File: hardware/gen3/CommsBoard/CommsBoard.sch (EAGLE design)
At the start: 47 parts, among them M5LOCK IMU_HEADER, U1 ATMEGA165PV-8AU

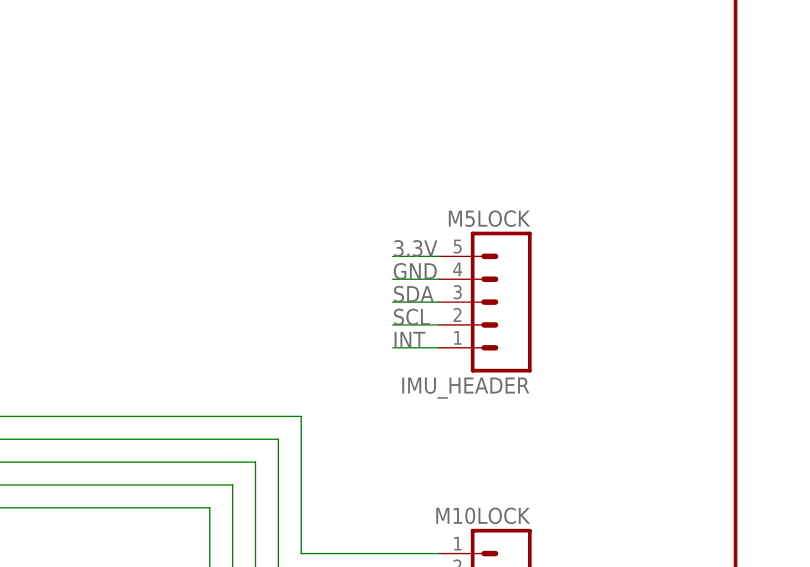
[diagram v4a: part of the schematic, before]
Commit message: Added IMU package
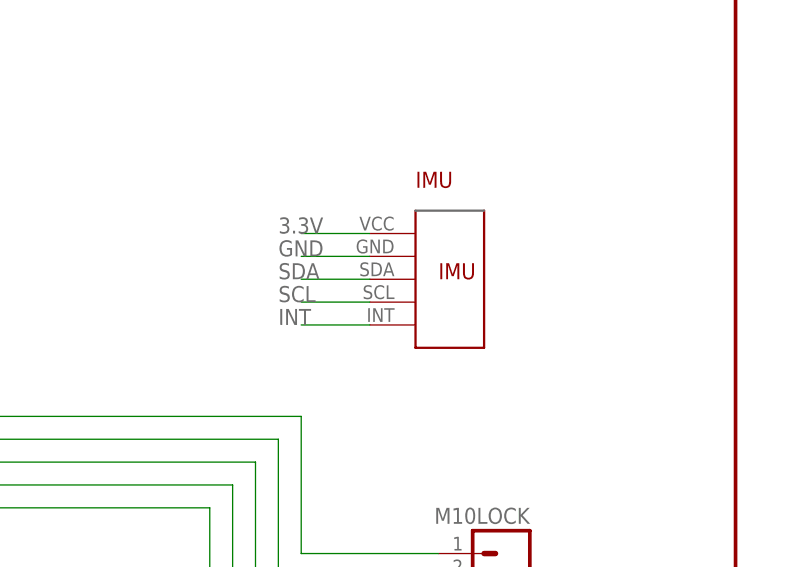
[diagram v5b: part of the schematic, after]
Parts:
- removed M5LOCK: IMU_HEADER, SparkFun-Connectors:M05LOCK
- added IMU: MPU6050IMUMPU, gen3:MPU6050IMUMPU
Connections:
- net 3.3V: now also IMU.VCC; no longer M5LOCK.5
- net GND: now also IMU.GND; no longer M5LOCK.4
- net INT: now also IMU.INT; no longer M5LOCK.1
- net SCL: now also IMU.SCL; no longer M5LOCK.2
- net SDA: now also IMU.SDA; no longer M5LOCK.3
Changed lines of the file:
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@@
 <part name="S1" library="SparkFun-Electromechanical" deviceset="SWITCH-MOMENTARY-2" device="SMD-4"/>
 <part name="R21" library="SparkFun-Passives" deviceset="RESISTOR" device="0805-RES" value="10k"/>
-<part name="M5LOCK" library="SparkFun-Connectors" deviceset="M05" device="LOCK" value="IMU_HEADER"/>
+<part name="IMU" library="gen3" deviceset="MPU6050IMU" device="MPU"/>
 </parts>
 <sheets>
@@
 <instance part="S1" gate="G$1" x="170.18" y="144.78"/>
 <instance part="R21" gate="G$1" x="172.72" y="132.08"/>
-<instance part="M5LOCK" gate="G$1" x="223.52" y="93.98" rot="MR0"/>
+<instance part="IMU" gate="G$1" x="215.9" y="96.52"/>
 </instances>
 <busses>
@@
 </segment>
 <segment>
-<pinref part="M5LOCK" gate="G$1" pin="4"/>
-<wire x1="215.9" y1="96.52" x2="210.82" y2="96.52" width="0.1524" layer="91"/>
-<label x="210.82" y="96.52" size="1.778" layer="95"/>
+<pinref part="IMU" gate="G$1" pin="GND"/>
+<wire x1="208.28" y1="99.06" x2="200.66" y2="99.06" width="0.1524" layer="91"/>
+<label x="198.12" y="99.06" size="1.778" layer="95"/>
 </segment>
 </net>
@@
 </segment>
 <segment>
-<pinref part="M5LOCK" gate="G$1" pin="5"/>
-<wire x1="215.9" y1="99.06" x2="210.82" y2="99.06" width="0.1524" layer="91"/>
-<label x="210.82" y="99.06" size="1.778" layer="95"/>
+<pinref part="IMU" gate="G$1" pin="VCC"/>
+<wire x1="208.28" y1="101.6" x2="200.66" y2="101.6" width="0.1524" layer="91"/>
+<label x="198.12" y="101.6" size="1.778" layer="95"/>
 </segment>
 </net>
@@
 </segment>
 <segment>
-<pinref part="M5LOCK" gate="G$1" pin="1"/>
-<wire x1="215.9" y1="88.9" x2="210.82" y2="88.9" width="0.1524" layer="91"/>
-<label x="210.82" y="88.9" size="1.778" layer="95"/>
+<pinref part="IMU" gate="G$1" pin="INT"/>
+<wire x1="208.28" y1="91.44" x2="200.66" y2="91.44" width="0.1524" layer="91"/>
+<label x="198.12" y="91.44" size="1.778" layer="95"/>
 </segment>
 </net>
@@
 </segment>
 <segment>
-<pinref part="M5LOCK" gate="G$1" pin="2"/>
-<wire x1="215.9" y1="91.44" x2="210.82" y2="91.44" width="0.1524" layer="91"/>
-<label x="210.82" y="91.44" size="1.778" layer="95"/>
+<pinref part="IMU" gate="G$1" pin="SCL"/>
+<wire x1="208.28" y1="93.98" x2="200.66" y2="93.98" width="0.1524" layer="91"/>
+<label x="198.12" y="93.98" size="1.778" layer="95"/>
 </segment>
 </net>
@@
 </segment>
 <segment>
-<pinref part="M5LOCK" gate="G$1" pin="3"/>
-<wire x1="215.9" y1="93.98" x2="210.82" y2="93.98" width="0.1524" layer="91"/>
-<label x="210.82" y="93.98" size="1.778" layer="95"/>
-</segment>
-</net>
+<pinref part="IMU" gate="G$1" pin="SDA"/>
+<wire x1="208.28" y1="96.52" x2="200.66" y2="96.52" width="0.1524" layer="91"/>
+<label x="198.12" y="96.52" size="1.778" layer="95"/>
+</segment>
+</net>

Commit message: finalized comms board
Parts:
- added C3, C4: 100uF, gen3:CAP-POLAR
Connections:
- net 3.3V: now also C3.+
- net 5V: now also C4.+
- net GND: now also C3.-, C4.-
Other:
- moved on the sheet: C5, C6
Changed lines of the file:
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@@
 <?xml version="1.0" encoding="utf-8"?>
 <!DOCTYPE eagle SYSTEM "eagle.dtd">
-<eagle version="7.2.0">
+<eagle version="6.4">
 <drawing>
 <settings>
@@
 <part name="R21" library="SparkFun-Passives" deviceset="RESISTOR" device="0805-RES" value="10k"/>
 <part name="IMU" library="gen3" deviceset="MPU6050IMU" device="MPU"/>
+<part name="C3" library="gen3" deviceset="CAP-POLAR" device="" value="100uF"/>
+<part name="C4" library="gen3" deviceset="CAP-POLAR" device="" value="100uF"/>
 </parts>
 <sheets>
@@
 <instance part="U1" gate="A" x="129.54" y="106.68"/>
 <instance part="JP1" gate="G$1" x="76.2" y="38.1"/>
-<instance part="C5" gate="G$1" x="63.5" y="152.4"/>
-<instance part="C6" gate="G$1" x="50.8" y="152.4"/>
+<instance part="C5" gate="G$1" x="66.04" y="154.94"/>
+<instance part="C6" gate="G$1" x="48.26" y="152.4"/>
 <instance part="U$2" gate="G$1" x="414.02" y="114.3"/>
 <instance part="S1" gate="G$1" x="170.18" y="144.78"/>
 <instance part="R21" gate="G$1" x="172.72" y="132.08"/>
 <instance part="IMU" gate="G$1" x="215.9" y="96.52"/>
+<instance part="C3" gate="G$1" x="55.88" y="154.94"/>
+<instance part="C4" gate="G$1" x="76.2" y="157.48"/>
 </instances>
 <busses>
@@
 <junction x="35.56" y="149.86"/>
 <pinref part="C6" gate="G$1" pin="2"/>
-<wire x1="35.56" y1="149.86" x2="50.8" y2="149.86" width="0.1524" layer="91"/>
+<wire x1="35.56" y1="149.86" x2="48.26" y2="149.86" width="0.1524" layer="91"/>
+<wire x1="48.26" y1="149.86" x2="55.88" y2="149.86" width="0.1524" layer="91"/>
+<junction x="48.26" y="149.86"/>
+<pinref part="C3" gate="G$1" pin="-"/>
+<pinref part="C4" gate="G$1" pin="-"/>
 <pinref part="C5" gate="G$1" pin="2"/>
-<wire x1="50.8" y1="149.86" x2="63.5" y2="149.86" width="0.1524" layer="91"/>
-<junction x="50.8" y="149.86"/>
+<wire x1="76.2" y1="152.4" x2="66.04" y2="152.4" width="0.1524" layer="91"/>
+<wire x1="66.04" y1="152.4" x2="66.04" y2="149.86" width="0.1524" layer="91"/>
+<junction x="66.04" y="152.4"/>
+<wire x1="66.04" y1="149.86" x2="55.88" y2="149.86" width="0.1524" layer="91"/>
+<junction x="55.88" y="149.86"/>
 </segment>
 <segment>
@@
 <wire x1="35.56" y1="157.48" x2="35.56" y2="154.94" width="0.1524" layer="91"/>
 <pinref part="C6" gate="G$1" pin="1"/>
-<wire x1="35.56" y1="157.48" x2="50.8" y2="157.48" width="0.1524" layer="91"/>
+<wire x1="35.56" y1="157.48" x2="48.26" y2="157.48" width="0.1524" layer="91"/>
 <junction x="35.56" y="157.48"/>
+<pinref part="C3" gate="G$1" pin="+"/>
+<wire x1="55.88" y1="157.48" x2="48.26" y2="157.48" width="0.1524" layer="91"/>
+<junction x="48.26" y="157.48"/>
 </segment>
 <segment>
@@
 <wire x1="35.56" y1="162.56" x2="35.56" y2="160.02" width="0.1524" layer="91"/>
 <junction x="35.56" y="160.02"/>
+<wire x1="35.56" y1="160.02" x2="66.04" y2="160.02" width="0.1524" layer="91"/>
 <pinref part="C5" gate="G$1" pin="1"/>
-<wire x1="35.56" y1="160.02" x2="63.5" y2="160.02" width="0.1524" layer="91"/>
-<wire x1="63.5" y1="160.02" x2="63.5" y2="157.48" width="0.1524" layer="91"/>
-</segment>
-</net>
+<pinref part="C4" gate="G$1" pin="+"/>
+<wire x1="66.04" y1="160.02" x2="76.2" y2="160.02" width="0.1524" layer="91"/>
+<junction x="66.04" y="160.02"/>
+</segment>
+</net>

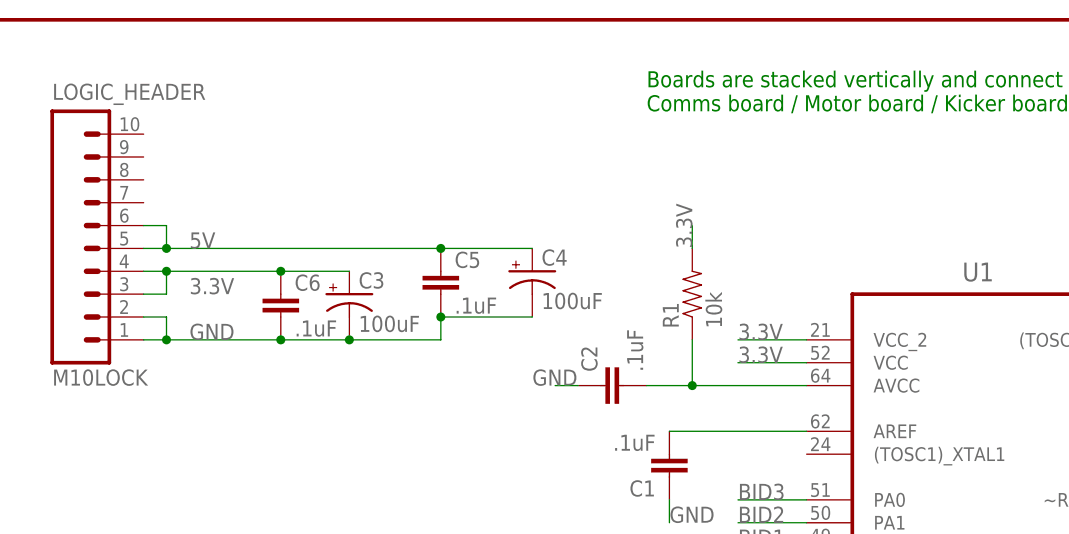
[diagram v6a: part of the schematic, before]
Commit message: added decoupling to comms and kicker
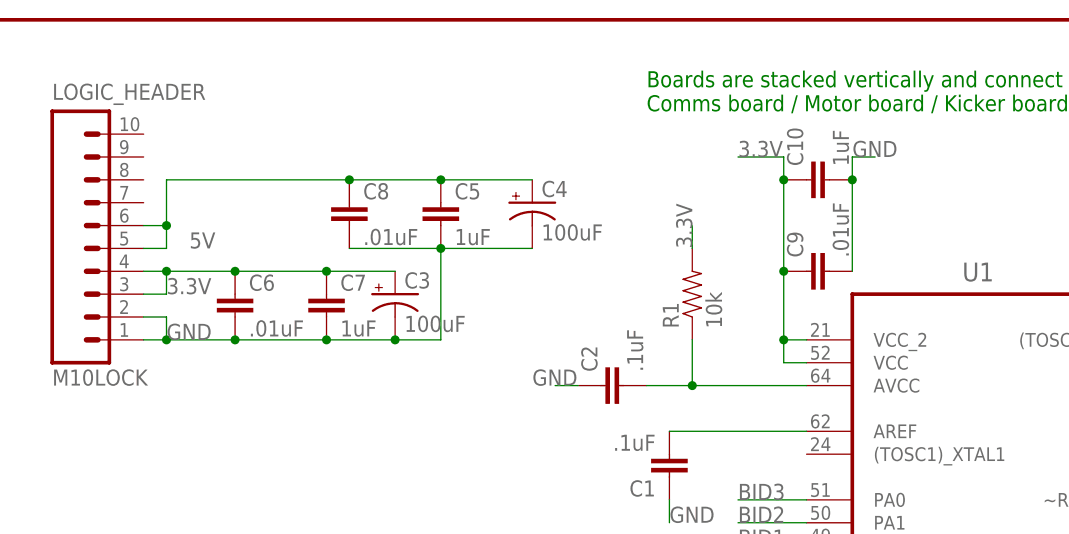
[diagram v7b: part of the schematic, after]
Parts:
- added C10, C7: 1uF, SparkFun-Capacitors:CAP0805
- added C8, C9: .01uF, SparkFun-Capacitors:CAP0805
- C5: value .1uF -> 1uF
- C6: value .1uF -> .01uF
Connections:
- net 3.3V: now also C10.1, C7.1, C9.1
- net 5V: now also C8.1
- net GND: now also C10.2, C7.2, C8.2, C9.2
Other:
- moved on the sheet: C3, C4, C5, C6
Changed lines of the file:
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@@
 <part name="U1" library="gen3" deviceset="ATMEGA165PV-8AU" device=""/>
 <part name="JP1" library="SparkFun-Connectors" deviceset="M05X2" device="PTH"/>
-<part name="C5" library="SparkFun-Capacitors" deviceset="CAP" device="0805" value=".1uF"/>
-<part name="C6" library="SparkFun-Capacitors" deviceset="CAP" device="0805" value=".1uF"/>
+<part name="C5" library="SparkFun-Capacitors" deviceset="CAP" device="0805" value="1uF"/>
+<part name="C6" library="SparkFun-Capacitors" deviceset="CAP" device="0805" value=".01uF"/>
 <part name="U$2" library="SparkFun-Sensors" deviceset="MCP9700" device="SMD"/>
 <part name="S1" library="SparkFun-Electromechanical" deviceset="SWITCH-MOMENTARY-2" device="SMD-4"/>
@@
 <part name="C3" library="gen3" deviceset="CAP-POLAR" device="" value="100uF"/>
 <part name="C4" library="gen3" deviceset="CAP-POLAR" device="" value="100uF"/>
+<part name="C7" library="SparkFun-Capacitors" deviceset="CAP" device="0805" value="1uF"/>
+<part name="C8" library="SparkFun-Capacitors" deviceset="CAP" device="0805" value=".01uF"/>
+<part name="C9" library="SparkFun-Capacitors" deviceset="CAP" device="0805" value=".01uF"/>
+<part name="C10" library="SparkFun-Capacitors" deviceset="CAP" device="0805" value="1uF"/>
 </parts>
 <sheets>
@@
 <instance part="U1" gate="A" x="129.54" y="106.68"/>
 <instance part="JP1" gate="G$1" x="76.2" y="38.1"/>
-<instance part="C5" gate="G$1" x="66.04" y="154.94"/>
-<instance part="C6" gate="G$1" x="48.26" y="152.4"/>
+<instance part="C5" gate="G$1" x="66.04" y="162.56"/>
+<instance part="C6" gate="G$1" x="43.18" y="152.4"/>
 <instance part="U$2" gate="G$1" x="414.02" y="114.3"/>
 <instance part="S1" gate="G$1" x="170.18" y="144.78"/>
 <instance part="R21" gate="G$1" x="172.72" y="132.08"/>
 <instance part="IMU" gate="G$1" x="215.9" y="96.52"/>
-<instance part="C3" gate="G$1" x="55.88" y="154.94"/>
-<instance part="C4" gate="G$1" x="76.2" y="157.48"/>
+<instance part="C3" gate="G$1" x="60.96" y="154.94"/>
+<instance part="C4" gate="G$1" x="76.2" y="165.1"/>
+<instance part="C7" gate="G$1" x="53.34" y="152.4"/>
+<instance part="C8" gate="G$1" x="55.88" y="162.56"/>
+<instance part="C9" gate="G$1" x="109.22" y="157.48" rot="R90"/>
+<instance part="C10" gate="G$1" x="109.22" y="167.64" rot="R90"/>
 </instances>
 <busses>
@@
 </segment>
 <segment>
-<label x="38.1" y="149.86" size="1.778" layer="95"/>
+<label x="35.56" y="149.86" size="1.778" layer="95"/>
 <pinref part="LOGIC_HEADER" gate="G$1" pin="2"/>
 <wire x1="33.02" y1="152.4" x2="35.56" y2="152.4" width="0.1524" layer="91"/>
@@
 <junction x="35.56" y="149.86"/>
 <pinref part="C6" gate="G$1" pin="2"/>
-<wire x1="35.56" y1="149.86" x2="48.26" y2="149.86" width="0.1524" layer="91"/>
-<wire x1="48.26" y1="149.86" x2="55.88" y2="149.86" width="0.1524" layer="91"/>
-<junction x="48.26" y="149.86"/>
+<wire x1="35.56" y1="149.86" x2="43.18" y2="149.86" width="0.1524" layer="91"/>
+<wire x1="43.18" y1="149.86" x2="53.34" y2="149.86" width="0.1524" layer="91"/>
+<junction x="43.18" y="149.86"/>
 <pinref part="C3" gate="G$1" pin="-"/>
 <pinref part="C4" gate="G$1" pin="-"/>
 <pinref part="C5" gate="G$1" pin="2"/>
-<wire x1="76.2" y1="152.4" x2="66.04" y2="152.4" width="0.1524" layer="91"/>
-<wire x1="66.04" y1="152.4" x2="66.04" y2="149.86" width="0.1524" layer="91"/>
-<junction x="66.04" y="152.4"/>
-<wire x1="66.04" y1="149.86" x2="55.88" y2="149.86" width="0.1524" layer="91"/>
-<junction x="55.88" y="149.86"/>
+<wire x1="53.34" y1="149.86" x2="60.96" y2="149.86" width="0.1524" layer="91"/>
+<wire x1="76.2" y1="160.02" x2="66.04" y2="160.02" width="0.1524" layer="91"/>
+<wire x1="66.04" y1="160.02" x2="66.04" y2="149.86" width="0.1524" layer="91"/>
+<junction x="66.04" y="160.02"/>
+<wire x1="66.04" y1="149.86" x2="60.96" y2="149.86" width="0.1524" layer="91"/>
+<junction x="60.96" y="149.86"/>
+<pinref part="C7" gate="G$1" pin="2"/>
+<junction x="53.34" y="149.86"/>
+<pinref part="C8" gate="G$1" pin="2"/>
+<wire x1="66.04" y1="160.02" x2="55.88" y2="160.02" width="0.1524" layer="91"/>
 </segment>
 <segment>
@@
 <label x="198.12" y="99.06" size="1.778" layer="95"/>
 </segment>
+<segment>
+<pinref part="C9" gate="G$1" pin="2"/>
+<pinref part="C10" gate="G$1" pin="2"/>
+<wire x1="111.76" y1="157.48" x2="111.76" y2="167.64" width="0.1524" layer="91"/>
+<wire x1="111.76" y1="167.64" x2="111.76" y2="170.18" width="0.1524" layer="91"/>
+<junction x="111.76" y="167.64"/>
+<wire x1="111.76" y1="170.18" x2="114.3" y2="170.18" width="0.1524" layer="91"/>
+<label x="111.76" y="170.18" size="1.778" layer="95"/>
+</segment>
 </net>
 <net name="3.3V" class="0">
@@
 <pinref part="LOGIC_HEADER" gate="G$1" pin="3"/>
 <wire x1="33.02" y1="154.94" x2="35.56" y2="154.94" width="0.1524" layer="91"/>
-<label x="38.1" y="154.94" size="1.778" layer="95"/>
+<label x="35.56" y="154.94" size="1.778" layer="95"/>
 <pinref part="LOGIC_HEADER" gate="G$1" pin="4"/>
 <wire x1="33.02" y1="157.48" x2="35.56" y2="157.48" width="0.1524" layer="91"/>
 <wire x1="35.56" y1="157.48" x2="35.56" y2="154.94" width="0.1524" layer="91"/>
 <pinref part="C6" gate="G$1" pin="1"/>
-<wire x1="35.56" y1="157.48" x2="48.26" y2="157.48" width="0.1524" layer="91"/>
+<wire x1="35.56" y1="157.48" x2="43.18" y2="157.48" width="0.1524" layer="91"/>
 <junction x="35.56" y="157.48"/>
 <pinref part="C3" gate="G$1" pin="+"/>
-<wire x1="55.88" y1="157.48" x2="48.26" y2="157.48" width="0.1524" layer="91"/>
-<junction x="48.26" y="157.48"/>
+<wire x1="60.96" y1="157.48" x2="53.34" y2="157.48" width="0.1524" layer="91"/>
+<junction x="43.18" y="157.48"/>
+<pinref part="C7" gate="G$1" pin="1"/>
+<wire x1="53.34" y1="157.48" x2="43.18" y2="157.48" width="0.1524" layer="91"/>
+<junction x="53.34" y="157.48"/>
 </segment>
 <segment>
@@
 </segment>
 <segment>
-<wire x1="106.68" y1="149.86" x2="99.06" y2="149.86" width="0.1524" layer="91"/>
-<label x="99.06" y="149.86" size="1.778" layer="95"/>
+<wire x1="106.68" y1="147.32" x2="104.14" y2="147.32" width="0.1524" layer="91"/>
+<label x="99.06" y="170.18" size="1.778" layer="95"/>
+<pinref part="U1" gate="A" pin="VCC"/>
+<wire x1="106.68" y1="149.86" x2="104.14" y2="149.86" width="0.1524" layer="91"/>
 <pinref part="U1" gate="A" pin="VCC_2"/>
-</segment>
-<segment>
-<wire x1="106.68" y1="147.32" x2="99.06" y2="147.32" width="0.1524" layer="91"/>
-<label x="99.06" y="147.32" size="1.778" layer="95"/>
-<pinref part="U1" gate="A" pin="VCC"/>
+<wire x1="104.14" y1="147.32" x2="104.14" y2="149.86" width="0.1524" layer="91"/>
+<junction x="104.14" y="149.86"/>
+<pinref part="C9" gate="G$1" pin="1"/>
+<wire x1="104.14" y1="149.86" x2="104.14" y2="157.48" width="0.1524" layer="91"/>
+<pinref part="C10" gate="G$1" pin="1"/>
+<wire x1="104.14" y1="157.48" x2="104.14" y2="167.64" width="0.1524" layer="91"/>
+<junction x="104.14" y="157.48"/>
+<wire x1="104.14" y1="167.64" x2="104.14" y2="170.18" width="0.1524" layer="91"/>
+<junction x="104.14" y="167.64"/>
+<wire x1="104.14" y1="170.18" x2="99.06" y2="170.18" width="0.1524" layer="91"/>
 </segment>
 <segment>
@@
 <wire x1="33.02" y1="162.56" x2="35.56" y2="162.56" width="0.1524" layer="91"/>
 <wire x1="35.56" y1="162.56" x2="35.56" y2="160.02" width="0.1524" layer="91"/>
-<junction x="35.56" y="160.02"/>
-<wire x1="35.56" y1="160.02" x2="66.04" y2="160.02" width="0.1524" layer="91"/>
+<pinref part="C4" gate="G$1" pin="+"/>
 <pinref part="C5" gate="G$1" pin="1"/>
-<pinref part="C4" gate="G$1" pin="+"/>
-<wire x1="66.04" y1="160.02" x2="76.2" y2="160.02" width="0.1524" layer="91"/>
-<junction x="66.04" y="160.02"/>
-</segment>
-</net>
+<wire x1="76.2" y1="167.64" x2="66.04" y2="167.64" width="0.1524" layer="91"/>
+<pinref part="C8" gate="G$1" pin="1"/>
+<wire x1="66.04" y1="167.64" x2="55.88" y2="167.64" width="0.1524" layer="91"/>
+<junction x="66.04" y="167.64"/>
+<wire x1="55.88" y1="167.64" x2="35.56" y2="167.64" width="0.1524" layer="91"/>
+<wire x1="35.56" y1="167.64" x2="35.56" y2="162.56" width="0.1524" layer="91"/>
+<junction x="55.88" y="167.64"/>
+<junction x="35.56" y="162.56"/>
+</segment>
+</net>

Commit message: added logos. generated gerbers
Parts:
- added U$3: LOGO, gen3:LOGO
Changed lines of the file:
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@@
 <layer number="56" name="wert" color="7" fill="1" visible="no" active="no"/>
 <layer number="57" name="tCAD" color="7" fill="1" visible="no" active="no"/>
+<layer number="59" name="tCarbon" color="7" fill="1" visible="no" active="no"/>
+<layer number="60" name="bCarbon" color="7" fill="1" visible="no" active="no"/>
 <layer number="90" name="Modules" color="5" fill="1" visible="yes" active="yes"/>
 <layer number="91" name="Nets" color="2" fill="1" visible="yes" active="yes"/>
@@
 <layer number="127" name="_tValues" color="7" fill="1" visible="yes" active="yes"/>
 <layer number="128" name="_bValues" color="7" fill="1" visible="yes" active="yes"/>
+<layer number="129" name="Mask" color="7" fill="1" visible="yes" active="yes"/>
 <layer number="131" name="tAdjust" color="7" fill="1" visible="yes" active="yes"/>
 <layer number="132" name="bAdjust" color="7" fill="1" visible="yes" active="yes"/>
@@
 <layer number="251" name="SMDround" color="12" fill="11" visible="no" active="no"/>
 <layer number="254" name="cooling" color="7" fill="1" visible="yes" active="yes"/>
+<layer number="255" name="routoute" color="7" fill="1" visible="yes" active="yes"/>
 </layers>
 <schematic xreflabel="%F%N/%S.%C%R" xrefpart="/%S.%C%R">
@@
 <part name="C9" library="SparkFun-Capacitors" deviceset="CAP" device="0805" value=".01uF"/>
 <part name="C10" library="SparkFun-Capacitors" deviceset="CAP" device="0805" value="1uF"/>
+<part name="U$3" library="gen3" deviceset="LOGO" device=""/>
 </parts>
 <sheets>
@@
 <instance part="C9" gate="G$1" x="109.22" y="157.48" rot="R90"/>
 <instance part="C10" gate="G$1" x="109.22" y="167.64" rot="R90"/>
+<instance part="U$3" gate="G$1" x="25.4" y="127"/>
 </instances>
 <busses>
